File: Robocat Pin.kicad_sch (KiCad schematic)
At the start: 17 parts, among them SW1 SW_SPDT_MSM, U1 NE555P

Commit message: Finished schematic and footprint assignments...need to add battery cell holder link then begin pcb design
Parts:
- AND1: footprint (none) -> Custom Library:Dual 2-Input Positive-AND Gate
- SW1: footprint (none) -> Custom Library:Notch 1 SMD-3P,2.5x6mm DIP Switches ROHS
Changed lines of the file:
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@@
     (property "Reference" "SW1" (id 0) (at 86.487 67.31 0))
     (property "Value" "SW_SPDT_MSM" (id 1) (at 86.487 69.85 0))
-    (property "Footprint" "" (id 2) (at 86.36 74.93 0)
+    (property "Footprint" "Custom Library:Notch 1 SMD-3P,2.5x6mm DIP Switches ROHS" (id 2) (at 86.36 74.93 0)
       (effects (font (size 1.27 1.27)) hide)
     )
@@
       (effects (font (size 1.27 1.27)) (justify left))
     )
-    (property "Footprint" "" (id 2) (at 87.63 86.36 0)
+    (property "Footprint" "Custom Library:Dual 2-Input Positive-AND Gate" (id 2) (at 87.63 86.36 0)
       (effects (font (size 1.27 1.27)) hide)
     )
@@
     )
     (path "/aef306da-1895-4311-b114-e39b67ff83ff"
-      (reference "AND1") (unit 1) (value "7408x2") (footprint "")
+      (reference "AND1") (unit 1) (value "7408x2") (footprint "Custom Library:Dual 2-Input Positive-AND Gate")
     )
     (path "/2239a272-4fc2-467b-84f7-d15b7dfe8fb3"
@@
     )
     (path "/12b39ead-9fb9-47b9-8961-6a55da6228fb"
-      (reference "SW1") (unit 1) (value "SW_SPDT_MSM") (footprint "")
+      (reference "SW1") (unit 1) (value "SW_SPDT_MSM") (footprint "Custom Library:Notch 1 SMD-3P,2.5x6mm DIP Switches ROHS")
     )
     (path "/b71aec2b-2559-4a0c-ac35-eaccff4f47e2"

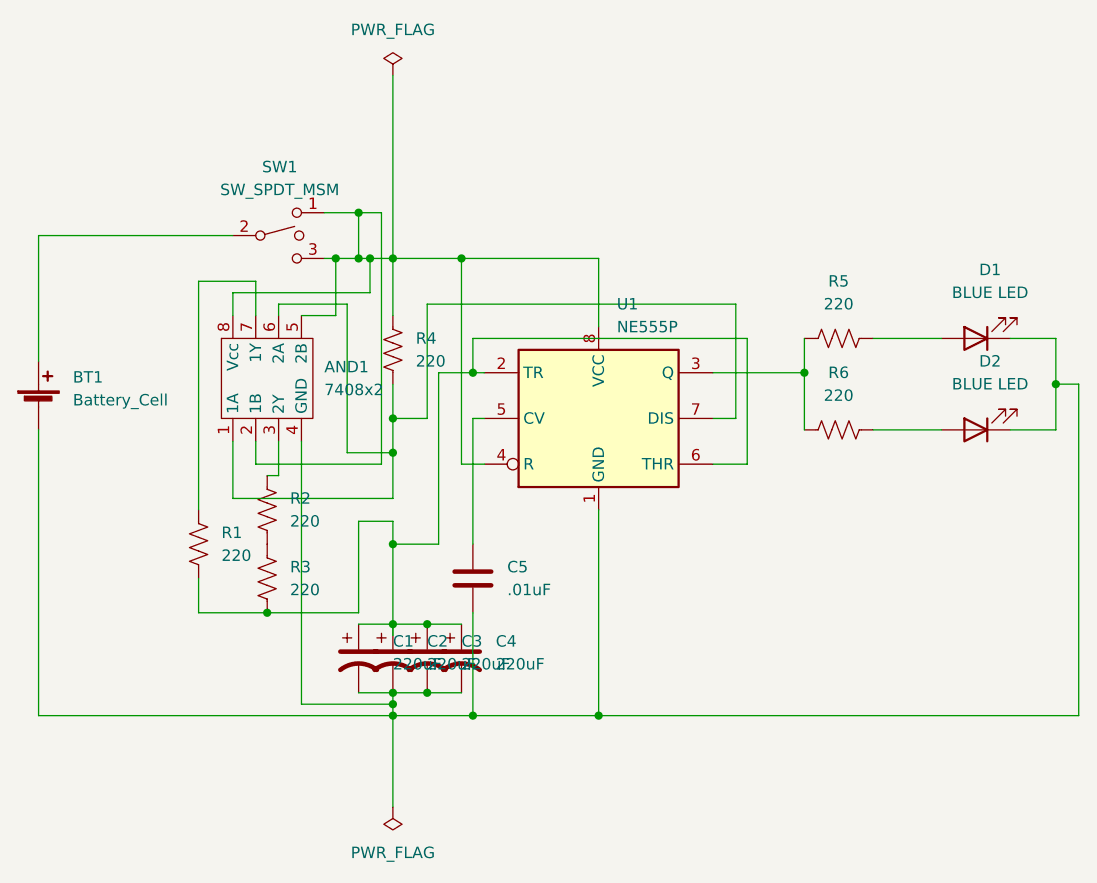
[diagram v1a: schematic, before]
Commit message: Redid the kicad circuit design to fit the update...need to reassign footprints and links, need to find new capacitor
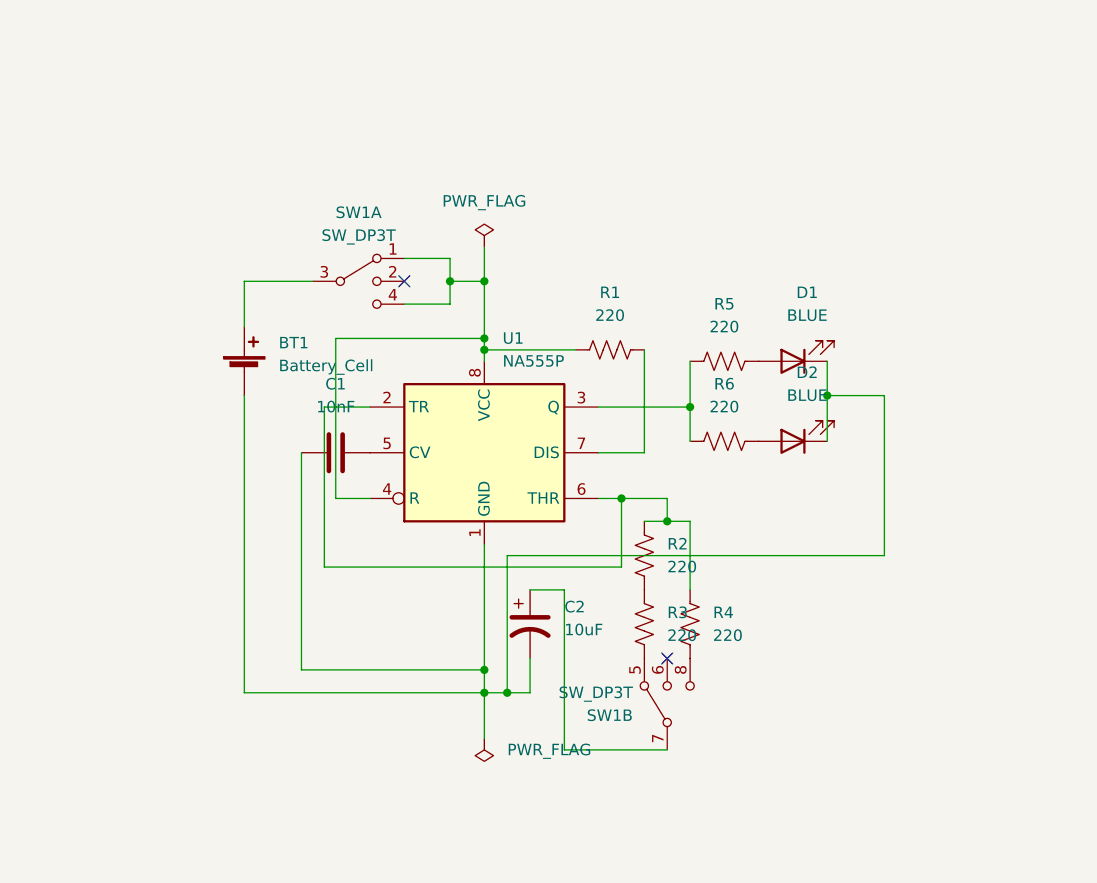
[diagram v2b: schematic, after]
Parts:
- removed AND1: 7408x2, Custom Library:Dual 2-Input Positive-AND Gate, symbol Custom Library:Dual_2-Input_AND_Gate
- removed C1, C3, C4: 220uF, Capacitor_SMD:CP_Elec_6.3x5.4, symbol Device:C_Polarized_US
- removed C5: .01uF, Capacitor_SMD:C_0402_1005Metric, symbol Device:C
- removed SW1: SW_SPDT_MSM, Custom Library:Notch 1 SMD-3P,2.5x6mm DIP Switches ROHS, symbol Switch:SW_SPDT_MSM
- removed U1: NE555P, Package_DIP:DIP-8_W7.62mm, symbol Timer:NE555P
- added C1: 10nF, symbol Device:C
- added SW1: SW_DP3T, symbol Switch:SW_DP3T
- added U1: NA555P, Package_DIP:DIP-8_W7.62mm, symbol Timer:NA555P
- BT1: footprint Battery:BatteryHolder_MPD_BC2003_1x2032 -> (none)
- C2: value 220uF -> 10uF; footprint Capacitor_SMD:CP_Elec_6.3x5.4 -> (none)
- D1, D2: value BLUE LED -> BLUE; footprint LED_SMD:LED_1206_3216Metric -> (none)
- R1, R2, R3, R4, R5, R6: footprint Resistor_SMD:R_0201_0603Metric -> (none)
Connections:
- net at R4.1: now also SW1.8
- net at BT1.1 (+): now also SW1.3
- net at BT1.2 (-), C2.2, D1.1 (K)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: now also C1.1, U1.1 (GND)
- net at R5.1, R6.1: now also U1.3 (Q)
- net at R2.1: now also R3.2
- net at R2.2: now also R4.2, U1.2 (TR), U1.6 (THR); no longer R3.1
- net at R1.1: now also SW1.1, SW1.4, U1.4 (R), U1.8 (VCC)
- new net: C1.2, U1.5 (CV)
- new net: R1.2, U1.7 (DIS)
- new net: R3.1, SW1.5
- new net: C2.1, SW1.7
- no-connect marks 0 -> 2

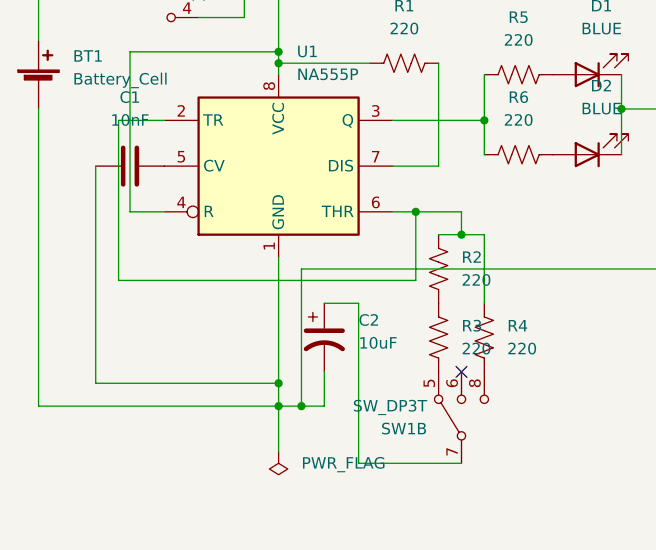
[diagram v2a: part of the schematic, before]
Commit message: Redid circuit, got all footprints done...need to make pcb design
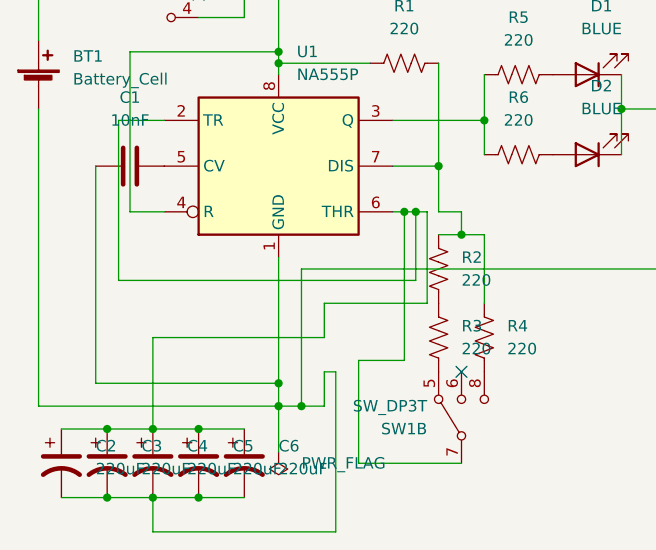
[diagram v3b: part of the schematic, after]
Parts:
- added C3, C4, C5, C6: 220uF, Capacitor_SMD:CP_Elec_6.3x5.4, symbol Device:C_Polarized_US
- BT1: footprint (none) -> Custom Library:2032 Battery Connector
- C1: footprint (none) -> Capacitor_SMD:C_0402_1005Metric
- C2: value 10uF -> 220uF; footprint (none) -> Capacitor_SMD:CP_Elec_6.3x5.4
- D1, D2: footprint (none) -> LED_SMD:LED_1206_3216Metric
- R1, R2, R3, R4, R5, R6: footprint (none) -> Resistor_SMD:R_0201_0603Metric
- SW1: footprint (none) -> Custom Library:DP3T Slide Switch
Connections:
- net at BT1.2 (-), C1.1, C2.2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: now also C3.2, C4.2, C5.2, C6.2
- net at U1.2 (TR), U1.6 (THR): now also C2.1, SW1.7, C3.1, C4.1, C5.1, C6.1; no longer R2.2, R4.2
- net at R1.2, U1.7 (DIS): now also R2.2, R4.2
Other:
- moved on the sheet: C2

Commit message: Made PCB, should be good to go now
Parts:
- D1, D2: footprint LED_SMD:LED_1206_3216Metric -> Custom Library:1.3x3.2mm LED
- U1: footprint Package_DIP:DIP-8_W7.62mm -> Custom Library:LM555CM
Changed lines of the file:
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@@
     (property "Reference" "D1" (id 0) (at 145.0975 81.28 0))
     (property "Value" "BLUE" (id 1) (at 145.0975 83.82 0))
-    (property "Footprint" "LED_SMD:LED_1206_3216Metric" (id 2) (at 143.51 88.9 0)
+    (property "Footprint" "Custom Library:1.3x3.2mm LED" (id 2) (at 143.51 88.9 0)
       (effects (font (size 1.27 1.27)) hide)
     )
@@
       (effects (font (size 1.27 1.27)) (justify left))
     )
-    (property "Footprint" "Package_DIP:DIP-8_W7.62mm" (id 2) (at 125.73 109.22 0)
-      (effects (font (size 1.27 1.27)) hide)
-    )
-    (property "Datasheet" "http://www.ti.com/lit/ds/symlink/ne555.pdf" (id 3) (at 130.81 109.22 0)
+    (property "Footprint" "Custom Library:LM555CM" (id 2) (at 125.73 109.22 0)
+      (effects (font (size 1.27 1.27)) hide)
+    )
+    (property "Datasheet" "https://www.lcsc.com/product-detail/Timers-Clock-Oscillators_HGSEMI-LM555CMM-TR_C5160086.html" (id 3) (at 130.81 109.22 0)
       (effects (font (size 1.27 1.27)) hide)
     )
@@
     (property "Reference" "D2" (id 0) (at 145.0975 90.17 0))
     (property "Value" "BLUE" (id 1) (at 145.0975 92.71 0))
-    (property "Footprint" "LED_SMD:LED_1206_3216Metric" (id 2) (at 143.51 97.79 0)
+    (property "Footprint" "Custom Library:1.3x3.2mm LED" (id 2) (at 143.51 97.79 0)
       (effects (font (size 1.27 1.27)) hide)
     )
@@
     )
     (path "/7f35b2a4-c774-457e-b5c9-0e4e4dac493a"
-      (reference "D1") (unit 1) (value "BLUE") (footprint "LED_SMD:LED_1206_3216Metric")
+      (reference "D1") (unit 1) (value "BLUE") (footprint "Custom Library:1.3x3.2mm LED")
     )
     (path "/a96120e9-d7bd-4936-9b8e-1051e9751107"
-      (reference "D2") (unit 1) (value "BLUE") (footprint "LED_SMD:LED_1206_3216Metric")
+      (reference "D2") (unit 1) (value "BLUE") (footprint "Custom Library:1.3x3.2mm LED")
     )
     (path "/e0cdf44c-3ee0-432d-ac41-707d8e8f7e04"
@@
     )
     (path "/8b4d3a25-1c34-4170-b4dc-82d23ede5625"
-      (reference "U1") (unit 1) (value "NA555P") (footprint "Package_DIP:DIP-8_W7.62mm")
-    )
-  )
+      (reference "U1") (unit 1) (value "NA555P") (footprint "Custom Library:LM555CM")
+    )
+  )

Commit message: Fixed footprints...need to fix pcb layout (batttery/leds), need to do pcb track
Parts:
- BT1: symbol Device:Battery_Cell -> Custom Library:Battery_Cell
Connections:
- net at C1.1, C2.2, C3.2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: now also BT1.1 (-); no longer BT1.2 (-)
- net at SW1.3: now also BT1.2 (+); no longer BT1.1 (+)
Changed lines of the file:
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@@
     (pin "2")
   )
-  (symbol (lib_id "Device:Battery_Cell") (at 82.55 90.17 0) (unit 1)
+  (symbol (lib_id "Custom Library:Battery_Cell") (at 82.55 90.17 0) (unit 1)
     (in_bom yes) (on_board yes) (fields_autoplaced)
     (property "Reference" "BT1" (id 0) (at 86.36 86.8679 0)
@@
       (effects (font (size 1.27 1.27)) (justify left))
     )
-    (property "Footprint" "Custom Library:2032 Battery Connector" (id 2) (at 82.55 88.646 90)
+    (property "Footprint" "Custom Library:2032 Battery Connector" (id 2) (at 87.63 87.63 90)
       (effects (font (size 1.27 1.27)) hide)
     )
-    (property "Datasheet" "https://www.lcsc.com/product-detail/span-style-background-color-ff0-Battery-span-Connectors_MYOUNG-MY-2032-12_C964833.html" (id 3) (at 82.55 88.646 90)
+    (property "Datasheet" "~" (id 3) (at 82.55 88.646 90)
       (effects (font (size 1.27 1.27)) hide)
     )

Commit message: Set all the traces
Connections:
- net gnd: now reaches BT1.1 (-), C1.1, C2.2, C3.2, C4.2, C5.2, C6.2, D1.1 (K), D2.1 (K), U1.1 (GND)
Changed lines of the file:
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@@
     (stroke (width 0) (type default) (color 0 0 0 0))
+  )
+  (label "gnd" (at 82.55 93.98 0)
+    (effects (font (size 1.27 1.27)) (justify left bottom))
   )
   (symbol (lib_id "Device:C_Polarized_US") (at 100.33 132.08 0) (unit 1)

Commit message: Worked on bom, working on redoing footprints for missing parts
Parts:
- BT1: value Battery_Cell -> Cell Battery; LCSC (none) -> C964833
- C1: LCSC (none) -> C60133
- C2, C3, C4, C5, C6: LCSC (none) -> C72494
- D1, D2: value BLUE -> Blue LED; LCSC (none) -> C3646934
- R1, R2, R3, R4, R5, R6: footprint Resistor_SMD:R_0201_0603Metric -> Custom Library:0603 Resistor; LCSC (none) -> C4355165
- SW1: value SW_DP3T -> DP3T Switch; LCSC (none) -> C2689537
- U1: value NA555P -> 555 Integrated Circuit; footprint Custom Library:LM555CM -> Custom Library:SOIC - 8 555; LCSC (none) -> C5160086
